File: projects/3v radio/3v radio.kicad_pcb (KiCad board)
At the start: 2 copper layers, 135.2 x 55 mm, 6 parts

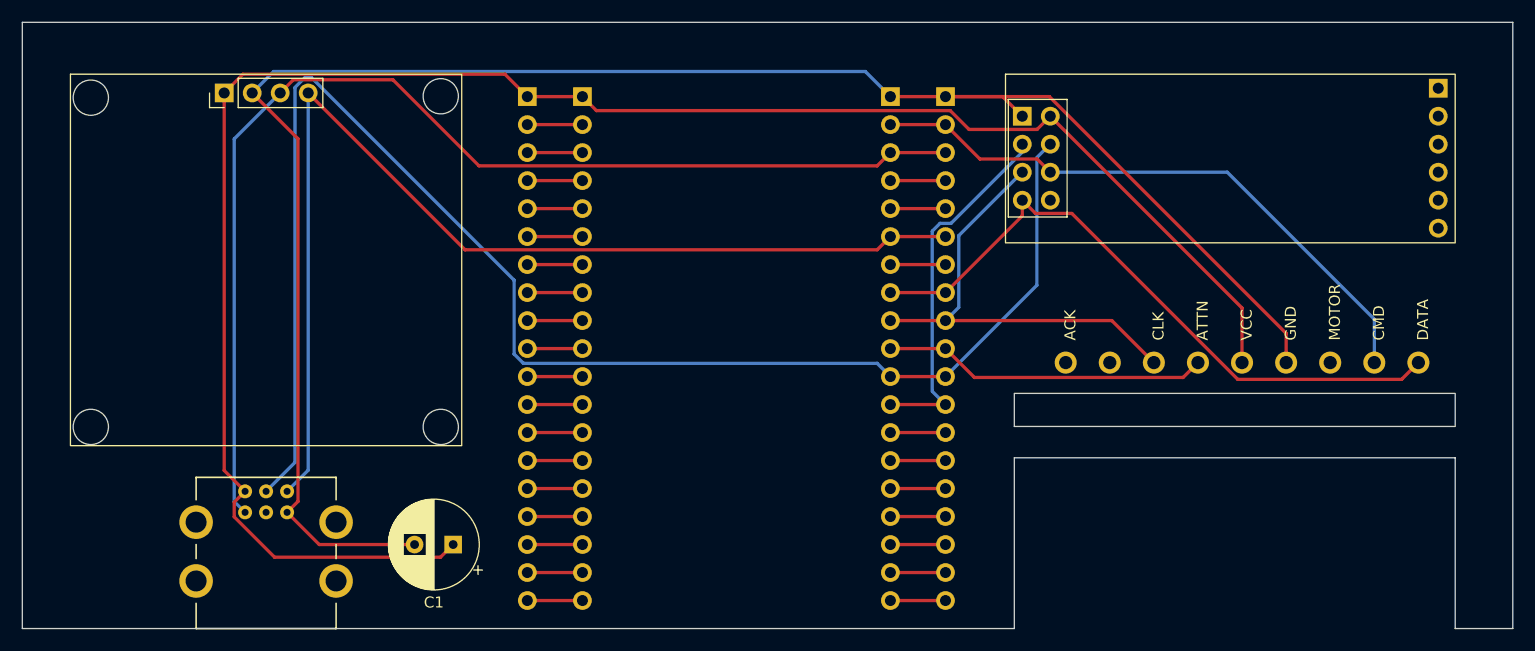
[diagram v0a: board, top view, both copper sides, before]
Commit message: 3v rad update
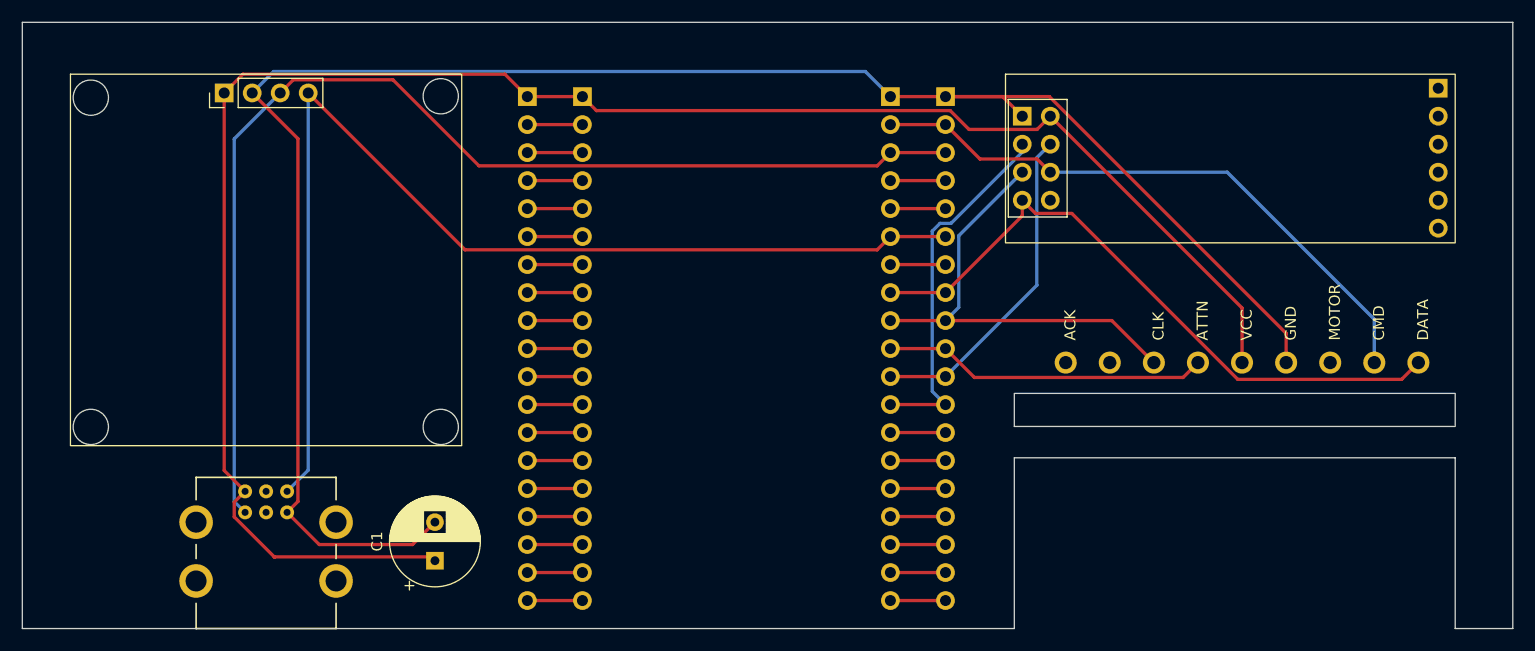
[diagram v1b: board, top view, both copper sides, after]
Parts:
- moved C1 2.21 mm to (123.7, 87.1), turned to 90 degrees
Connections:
- U2 pad 3: Net-(ESP32-WROOM-32U1-17) -> unconnected-(U2-Detect_device-Pad3)
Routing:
- net Net-(ESP32-WROOM-32U1-17): track 137.3 -> 30.0 mm
- net Net-(NRF1-GND): track 167.8 -> 170.5 mm
- net Net-(ESP32-WROOM-32U1-3.3v): track 169.3 -> 167.3 mm
